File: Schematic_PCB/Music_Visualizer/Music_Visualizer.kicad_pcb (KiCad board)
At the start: 2 copper layers, 295 x 155 mm, 238 parts, among them J1 AudioJack2_Ground, J2 PJ-079BH, SW1 SW_SPDT, SW2 SW_SPST, U1 LM324, U10 LM3915N-1, U11 LM3915N-1, U12 LM3915N-1, U13 LM3915N-1, U14 LM3915N-1, U15 LM3915N-1, U16 LM3915N-1, U17 NCP161ASN350T1G, U18 NCS333ASQ3T2G, U2 LM324, U3 LM324, U4 LM324, U5 LM324, U6 LM324, U7 LM324, U8 LT1054, U9 MC78L05_TO92

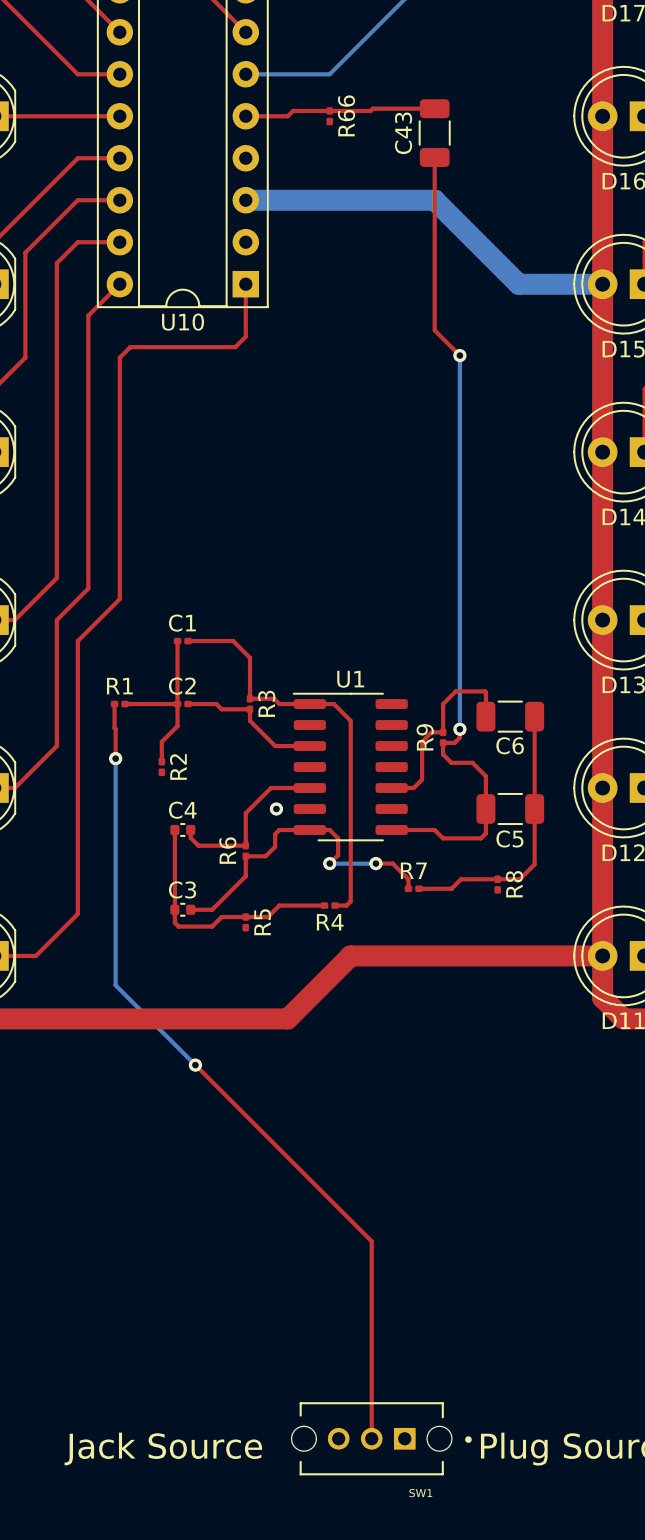
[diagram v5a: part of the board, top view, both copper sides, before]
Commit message: Found new way to rout internal filter stages, completed Sub-Bass filter, allows grounds to be connected and leaves spaces +/- 5V power
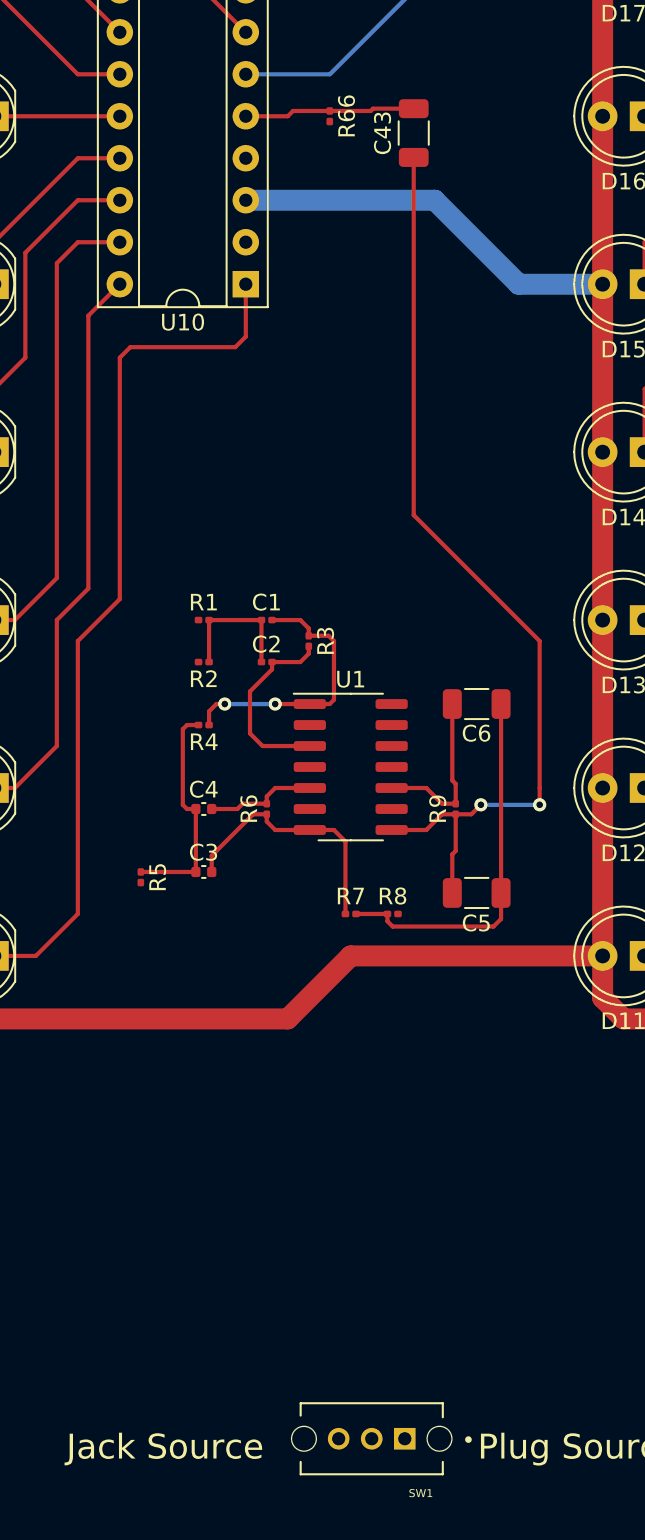
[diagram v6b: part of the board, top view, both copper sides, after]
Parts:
- moved R4 13.3 mm to (96.5, 125.7)
- moved R1 7.18 mm to (96.5, 119.4)
- moved R5 6.91 mm to (92.7, 134.9)
- moved R2 6.84 mm to (96.5, 121.9), turned to 180 degrees
- moved R8 6.59 mm to (108.0, 137.2), turned to 0 degrees
- moved C2 5.68 mm to (100.3, 121.9)
- moved C5 5.47 mm to (113.0, 135.9)
- moved C1 5.24 mm to (100.3, 119.4)
- moved R3 5.21 mm to (102.9, 120.7)
- moved R9 4.38 mm to (111.8, 130.8)
- moved R7 4.10 mm to (105.4, 137.2)
- moved R6 2.84 mm to (100.3, 130.8)
- moved C3 2.62 mm to (96.5, 134.6)
- moved C6 2.17 mm to (113.0, 124.5)
- moved C4 1.80 mm to (96.5, 130.8)
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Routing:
- net Vsig: track 50.9 -> 0.00 mm, vias 2 -> 0
- net Net-(C1-Pad2): track 25.3 -> 16.8 mm, vias 0 -> 2
- net Net-(C43-Pad1): track 50.2 -> 56.8 mm
- net Net-(C5-Pad1): track 16.6 -> 22.5 mm
- net Net-(C3-Pad2): track 19.7 -> 15.4 mm, vias 2 -> 0
- net Net-(C4-Pad2): track 10.5 -> 6.72 mm
- net Net-(C2-Pad2): track 8.82 -> 11.7 mm
- net Net-(C1-Pad1): track 10.9 -> 8.25 mm
- net Net-(C3-Pad1): track 15.3 -> 13.7 mm
- net Net-(C6-Pad2): track 12.0 -> 10.4 mm
- net VSubBass: track 11.6 -> 10.4 mm
- net GND: vias 1 -> 0

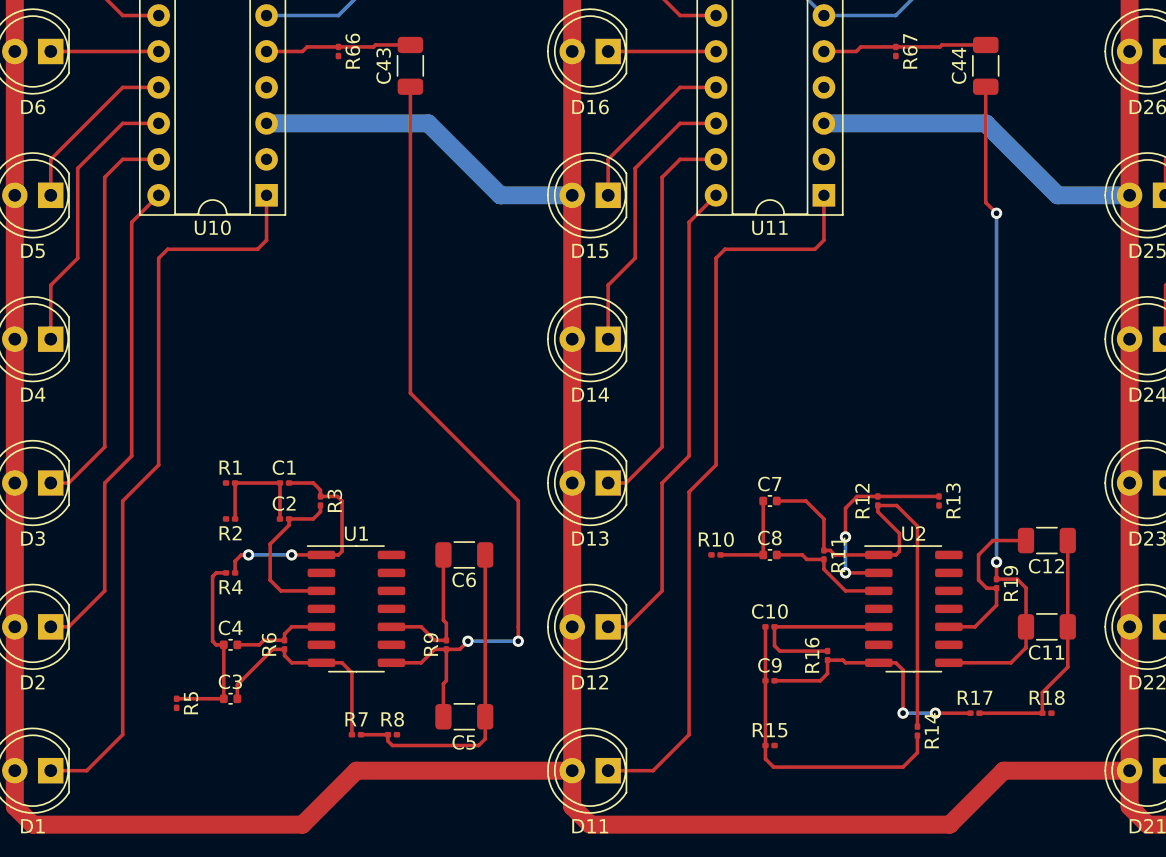
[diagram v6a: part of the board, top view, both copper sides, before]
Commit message: Finished Tracing bass filter
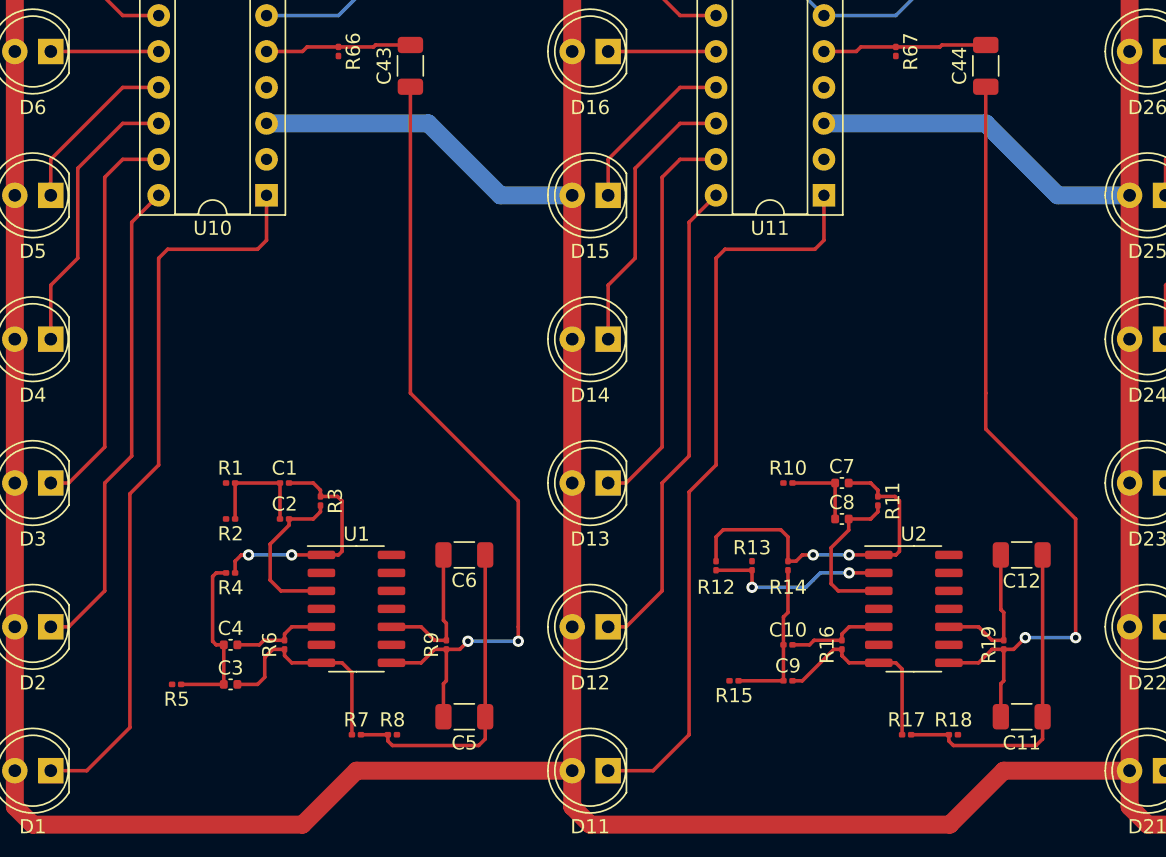
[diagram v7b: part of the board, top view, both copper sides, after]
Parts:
- moved R14 14.8 mm to (135.9, 125.2)
- moved R13 14.0 mm to (133.3, 125.2), turned to 90 degrees
- moved R12 12.3 mm to (130.8, 125.2), turned to -90 degrees
- moved R10 7.18 mm to (135.9, 119.4)
- moved R18 6.78 mm to (147.6, 137.2)
- moved C11 6.59 mm to (152.4, 135.9)
- moved C8 5.68 mm to (139.7, 121.9)
- moved R11 5.39 mm to (142.2, 120.7)
- moved C7 5.24 mm to (139.7, 119.4)
- moved R15 5.23 mm to (132.1, 133.3), turned to 180 degrees
- moved R17 5.06 mm to (144.3, 137.2)
- moved R19 4.35 mm to (151.1, 130.8), turned to 90 degrees
- moved C12 2.05 mm to (152.4, 124.5)
- moved C10 1.80 mm to (135.9, 130.8)
- moved R5 1.34 mm to (92.7, 133.6), turned to 180 degrees
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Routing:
- net Net-(C10-Pad1): track 21.9 -> 11.1 mm
- net Net-(C11-Pad2): track 47.5 -> 56.1 mm
- net Net-(U2-Pad1): track 33.1 -> 25.0 mm, vias 0 -> 2
- net Net-(C10-Pad2): track 12.6 -> 6.88 mm
- net Net-(C11-Pad1): track 17.4 -> 23.1 mm
- net Net-(C9-Pad2): track 18.3 -> 14.1 mm, vias 2 -> 0
- net Net-(U2-Pad3): track 8.66 -> 11.4 mm
- net Net-(C12-Pad2): track 12.3 -> 10.4 mm
- net Net-(C3-Pad1): track 13.7 -> 12.3 mm
- net Net-(C7-Pad1): track 6.82 -> 5.55 mm
- net Net-(R12-Pad2): track 13.9 -> 13.1 mm
